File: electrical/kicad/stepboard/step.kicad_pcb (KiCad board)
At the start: 2 copper layers, 139.7 x 76.2 mm, 80 parts, among them J1 Conn_02x03_Odd_Even, J10 Conn_02x03_Odd_Even, J11 Conn_02x03_Odd_Even, J12 Conn_02x03_Odd_Even, J13 Conn_01x04, J14 Conn_01x04, J15 Conn_01x04, J16 Conn_01x04, J17 Conn_01x04, J18 Conn_01x04, J19 Conn_01x04, J2 Conn_02x03_Odd_Even, J20 Conn_01x04, J21 Conn_01x04, J22 Conn_01x04, J23 Conn_01x04, J24 Conn_01x04, J25 Conn_02x12_Odd_Even, J26 Screw_Terminal_01x03, J3 Conn_02x03_Odd_Even, J4 Conn_02x03_Odd_Even, J5 Conn_02x03_Odd_Even, J6 Conn_02x03_Odd_Even, J7 Conn_02x03_Odd_Even, J8 Conn_02x03_Odd_Even, J9 Conn_02x03_Odd_Even, U1 MKS_TMC2209, U10 MKS_TMC2209, U11 MKS_TMC2209, U12 MKS_TMC2209, U2 MKS_TMC2209, U3 MKS_TMC2209, U4 MKS_TMC2209, U5 MKS_TMC2209, U6 MKS_TMC2209, U7 MKS_TMC2209, U8 MKS_TMC2209, U9 MKS_TMC2209

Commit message: update(kicad/pdb): sch with mobility components
- added rover mobility components to schematic
- added overcurrent and flyback protection ckt
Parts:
- J13, J14, J15, J16, J17, J18, J19, J20, J21, J22, J23, J24: footprint Connector_PinHeader_2.54mm:PinHeader_1x04_P2.54mm_Vertical -> Connectors_JST:JST_XH_1x04_P2.54mm_Vertical
- J26: footprint Connector_PinHeader_2.54mm:PinHeader_1x03_P2.54mm_Vertical -> Connectors_JST:JST_XH_1x03_P2.54mm_Vertical

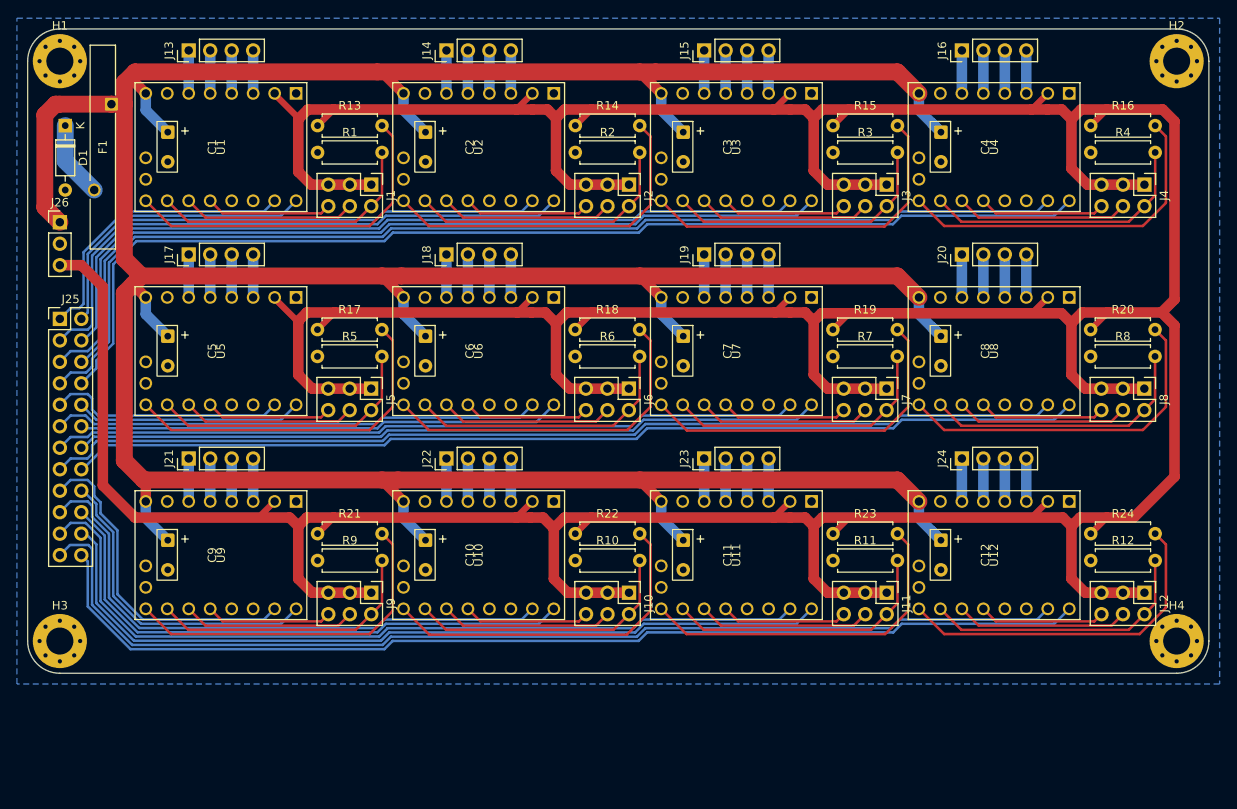
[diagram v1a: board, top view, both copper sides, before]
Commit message: update(kicad/step): reduce from 12 to 9 motors and optimize space
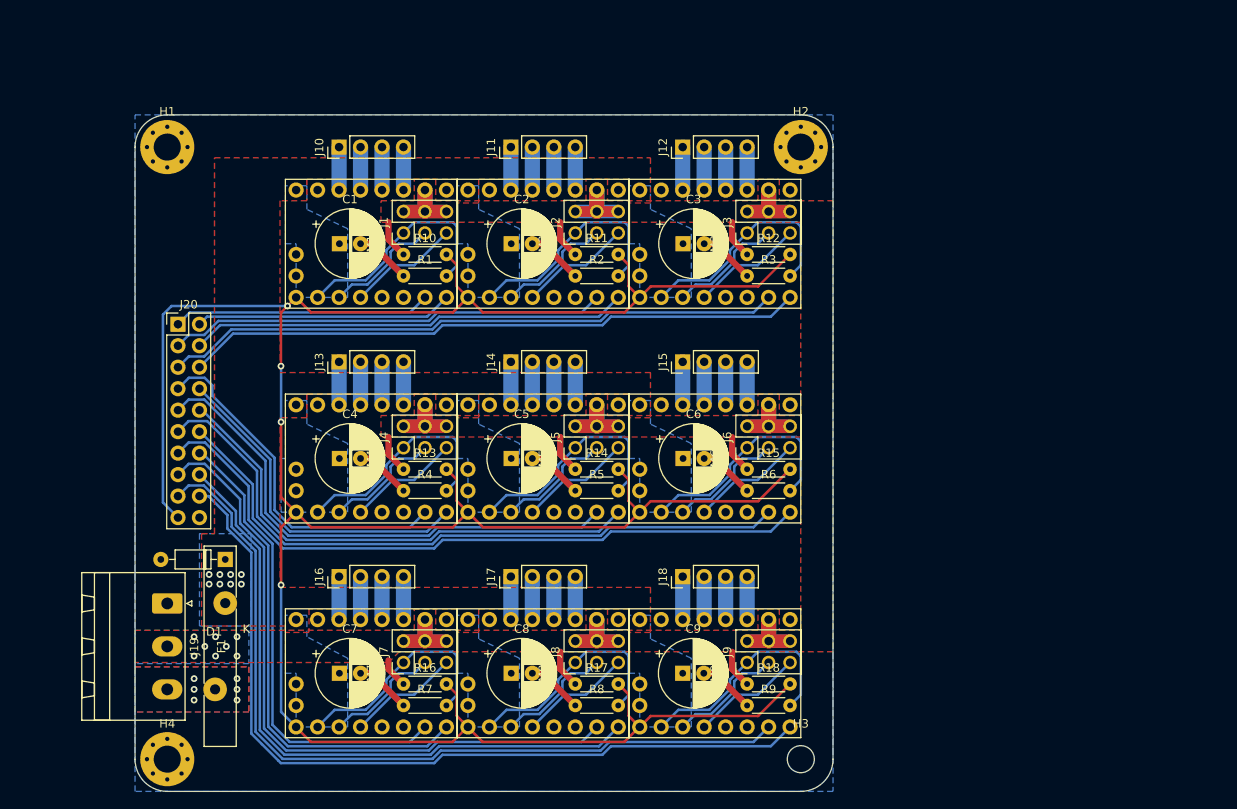
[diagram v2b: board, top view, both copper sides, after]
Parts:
- removed C10, C11, C12: 100uF, Capacitors_THT:CP_Radial_D8.0mm_P3.50mm_H12.0mm_Horizontal
- removed J21, J22, J23, J24: Conn_01x04, Connectors_JST:JST_XH_1x04_P2.54mm_Vertical
- removed J25: Conn_02x12_Odd_Even, Connector_PinHeader_2.54mm:PinHeader_2x12_P2.54mm_Vertical
- removed J26: Screw_Terminal_01x03, Connectors_JST:JST_XH_1x03_P2.54mm_Vertical
- removed R19, R20, R21, R22, R23, R24: 10k, Resistor_THT:R_Axial_DIN0207_L6.3mm_D2.5mm_P7.62mm_Horizontal
- removed U1, U10, U11, U12, U2, U3, U4, U5, U6, U7, U8, U9: MKS_TMC2209, Motor_Driver:MKS_TMC2209
- added M1: TMC22XX, Motor_Driver:MKS_TMC22XX, F.Cu at (62.2, 52.1)
- added M2: TMC22XX, Motor_Driver:MKS_TMC22XX, F.Cu at (82.5, 52.1)
- added M3: TMC22XX, Motor_Driver:MKS_TMC22XX, F.Cu at (102.9, 52.1)
- added M4: TMC22XX, Motor_Driver:MKS_TMC22XX, F.Cu at (62.2, 77.5)
- added M5: TMC22XX, Motor_Driver:MKS_TMC22XX, F.Cu at (82.5, 77.5)
- added M6: TMC22XX, Motor_Driver:MKS_TMC22XX, F.Cu at (102.9, 77.5)
- added M7: TMC22XX, Motor_Driver:MKS_TMC22XX, F.Cu at (62.2, 102.9)
- added M8: TMC22XX, Motor_Driver:MKS_TMC22XX, F.Cu at (82.5, 102.9)
- added M9: TMC22XX, Motor_Driver:MKS_TMC22XX, F.Cu at (102.9, 102.9)
- C1, C2, C3, C4, C5, C6, C7, C8, C9: value 100uF -> 100u; footprint Capacitors_THT:CP_Radial_D8.0mm_P3.50mm_H12.0mm_Horizontal -> Capacitor_THT:CP_Radial_D8.0mm_P2.50mm
- D1: value D -> D_Small
- F1: value Fuse -> Polyfuse_Small; footprint Fuses_THT:Fuse_Tyco-RUEF900 -> Fuses_THT:Fuse_Tyco_RGEF1400
- H3: value MountingHole_Pad -> MountingHole; footprint MountingHole:MountingHole_3.2mm_M3_Pad_Via -> MountingHole:MountingHole_3.2mm_M3
- J10, J11, J12: value Conn_02x03_Odd_Even -> Conn_01x04; footprint Connector_PinHeader_2.54mm:PinHeader_2x03_P2.54mm_Vertical -> Connectors_JST:JST_XH_1x04_P2.54mm_Vertical
- J19: value Conn_01x04 -> Screw_Terminal_01x03; footprint Connectors_JST:JST_XH_1x04_P2.54mm_Vertical -> Connector_Phoenix_MSTB:PhoenixContact_MSTBA_2,5_3-G-5,08_1x03_P5.08mm_Horizontal
- J20: value Conn_01x04 -> Conn_02x10_Odd_Even; footprint Connectors_JST:JST_XH_1x04_P2.54mm_Vertical -> Connector_PinHeader_2.54mm:PinHeader_2x10_P2.54mm_Vertical
- R1, R13, R14, R15, R16, R17, R18, R2, R3, R4, R5, R6, R7, R8, R9: footprint Resistor_THT:R_Axial_DIN0207_L6.3mm_D2.5mm_P7.62mm_Horizontal -> Resistor_THT:R_Axial_DIN0204_L3.6mm_D1.6mm_P5.08mm_Horizontal
- R10, R11, R12: value 100k -> 10k; footprint Resistor_THT:R_Axial_DIN0207_L6.3mm_D2.5mm_P7.62mm_Horizontal -> Resistor_THT:R_Axial_DIN0204_L3.6mm_D1.6mm_P5.08mm_Horizontal
- moved H4 120.2 mm to (38.1, 113.0)
- moved R16 104.7 mm to (66.0, 104.1)
- moved J16 96.4 mm to (58.4, 91.4)
- moved J20 93.1 mm to (39.4, 61.6), turned to 0 degrees
- moved J4 93.0 mm to (66.0, 76.2), turned to 90 degrees
- moved R4 90.6 mm to (66.0, 81.3)
- moved H3 88.7 mm to (113.0, 113.0)
- moved C4 80.9 mm to (58.5, 77.5), turned to 0 degrees
- moved J12 75.9 mm to (99.1, 40.6), turned to 90 degrees
- moved J19 75.7 mm to (38.1, 94.6), turned to -90 degrees
- moved J8 74.7 mm to (86.4, 101.6), turned to 90 degrees
- moved R8 73.6 mm to (86.4, 106.7)
- moved J11 68.9 mm to (78.7, 40.6), turned to 90 degrees
- moved J7 65.7 mm to (66.0, 101.6), turned to 90 degrees
- moved F1 65.5 mm to (43.8, 104.8), turned to 90 degrees
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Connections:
- C1 pad 2: GND -> /GND
- C2 pad 2: GND -> /GND
- C3 pad 2: GND -> /GND
- C4 pad 2: GND -> /GND
- C5 pad 2: GND -> /GND
- C6 pad 2: GND -> /GND
- C7 pad 2: GND -> /GND
- C8 pad 2: GND -> /GND
- C9 pad 2: GND -> /GND
- D1 pad 1: Net-(D1-K) -> /+12V
- D1 pad 2: GND -> /GND
- F1 pad 1: /+12V -> Net-(J19-Pin_3)
- F1 pad 2: Net-(D1-K) -> /+12V
- H1 pad 1: GND -> /GND
- H2 pad 1: GND -> /GND
- H4 pad 1: GND -> /GND
- J1 pad 1: +5V -> Net-(J1-Pin_1)
- J1 pad 2: Net-(J1-Pin_2) -> /+5V
- J1 pad 3: +5V -> Net-(J1-Pin_3)
- J1 pad 4: Net-(J1-Pin_4) -> /+5V
- J1 pad 5: +5V -> Net-(J1-Pin_5)
- J1 pad 6: Net-(J1-Pin_6) -> /+5V
- J10 pad 1: +5V -> Net-(J10-Pin_1)
- J10 pad 3: +5V -> Net-(J10-Pin_3)
- J11 pad 1: +5V -> Net-(J11-Pin_1)
- J11 pad 3: +5V -> Net-(J11-Pin_3)
- J12 pad 1: +5V -> Net-(J12-Pin_1)
- J12 pad 3: +5V -> Net-(J12-Pin_3)
- J19 pad 1: Net-(J19-Pin_1) -> /GND
- J19 pad 2: Net-(J19-Pin_2) -> /+5V
- J2 pad 1: +5V -> Net-(J2-Pin_1)
- J2 pad 2: Net-(J2-Pin_2) -> /+5V
- J2 pad 3: +5V -> Net-(J2-Pin_3)
- J2 pad 4: Net-(J2-Pin_4) -> /+5V
- J2 pad 5: +5V -> Net-(J2-Pin_5)
- J2 pad 6: Net-(J2-Pin_6) -> /+5V
- J20 pad 1: Net-(J20-Pin_1) -> /ST1_STP
- J20 pad 2: Net-(J20-Pin_2) -> /ST1_DIR
- J20 pad 3: Net-(J20-Pin_3) -> /ST2_STP
- J20 pad 4: Net-(J20-Pin_4) -> /ST2_DIR
- J3 pad 1: +5V -> Net-(J3-Pin_1)
- J3 pad 2: Net-(J3-Pin_2) -> /+5V
- J3 pad 3: +5V -> Net-(J3-Pin_3)
- J3 pad 4: Net-(J3-Pin_4) -> /+5V
- J3 pad 5: +5V -> Net-(J3-Pin_5)
- J3 pad 6: Net-(J3-Pin_6) -> /+5V
- J4 pad 1: +5V -> Net-(J4-Pin_1)
- J4 pad 2: Net-(J4-Pin_2) -> /+5V
- J4 pad 3: +5V -> Net-(J4-Pin_3)
- J4 pad 4: Net-(J4-Pin_4) -> /+5V
- J4 pad 5: +5V -> Net-(J4-Pin_5)
- J4 pad 6: Net-(J4-Pin_6) -> /+5V
- J5 pad 1: +5V -> Net-(J5-Pin_1)
- J5 pad 2: Net-(J5-Pin_2) -> /+5V
- J5 pad 3: +5V -> Net-(J5-Pin_3)
- J5 pad 4: Net-(J5-Pin_4) -> /+5V
- J5 pad 5: +5V -> Net-(J5-Pin_5)
- J5 pad 6: Net-(J5-Pin_6) -> /+5V
- J6 pad 1: +5V -> Net-(J6-Pin_1)
- J6 pad 2: Net-(J6-Pin_2) -> /+5V
- J6 pad 3: +5V -> Net-(J6-Pin_3)
- J6 pad 4: Net-(J6-Pin_4) -> /+5V
- J6 pad 5: +5V -> Net-(J6-Pin_5)
- J6 pad 6: Net-(J6-Pin_6) -> /+5V
- J7 pad 1: +5V -> Net-(J7-Pin_1)
- J7 pad 2: Net-(J7-Pin_2) -> /+5V
- J7 pad 3: +5V -> Net-(J7-Pin_3)
- J7 pad 4: Net-(J7-Pin_4) -> /+5V
- J7 pad 5: +5V -> Net-(J7-Pin_5)
- J7 pad 6: Net-(J7-Pin_6) -> /+5V
- J8 pad 1: +5V -> Net-(J8-Pin_1)
- J8 pad 2: Net-(J8-Pin_2) -> /+5V
- J8 pad 3: +5V -> Net-(J8-Pin_3)
- J8 pad 4: Net-(J8-Pin_4) -> /+5V
- J8 pad 5: +5V -> Net-(J8-Pin_5)
- J8 pad 6: Net-(J8-Pin_6) -> /+5V
- J9 pad 1: +5V -> Net-(J9-Pin_1)
- J9 pad 2: Net-(J9-Pin_2) -> /+5V
- J9 pad 3: +5V -> Net-(J9-Pin_3)
- J9 pad 4: Net-(J9-Pin_4) -> /+5V
- J9 pad 5: +5V -> Net-(J9-Pin_5)
- J9 pad 6: Net-(J9-Pin_6) -> /+5V
- R1 pad 1: GND -> /GND
- R1 pad 2: Net-(J1-Pin_2) -> Net-(J1-Pin_1)
- R10 pad 1: GND -> /+5V
- R10 pad 2: Net-(J10-Pin_2) -> /STP_ENA
- R11 pad 1: GND -> /+5V
- R11 pad 2: Net-(J11-Pin_2) -> /STP_ENA
- R12 pad 1: GND -> /+5V
- R12 pad 2: Net-(J12-Pin_2) -> /STP_ENA
- R13 pad 1: +5V -> /+5V
- R13 pad 2: Net-(U1-~{EN}) -> /STP_ENA
- R14 pad 1: +5V -> /+5V
- R14 pad 2: Net-(U2-~{EN}) -> /STP_ENA
- R15 pad 1: +5V -> /+5V
- R15 pad 2: Net-(U3-~{EN}) -> /STP_ENA
- R16 pad 1: +5V -> /+5V
- R16 pad 2: Net-(U4-~{EN}) -> /STP_ENA
- R17 pad 1: +5V -> /+5V
- R17 pad 2: Net-(U5-~{EN}) -> /STP_ENA
- R18 pad 1: +5V -> /+5V
- R18 pad 2: Net-(U6-~{EN}) -> /STP_ENA
- R2 pad 1: GND -> /GND
- R2 pad 2: Net-(J2-Pin_2) -> Net-(J2-Pin_1)
- R3 pad 1: GND -> /GND
- R3 pad 2: Net-(J3-Pin_2) -> Net-(J3-Pin_1)
- R4 pad 1: GND -> /GND
- R4 pad 2: Net-(J4-Pin_2) -> Net-(J4-Pin_1)
- R5 pad 1: GND -> /GND
- R5 pad 2: Net-(J5-Pin_2) -> Net-(J5-Pin_1)
- R6 pad 1: GND -> /GND
- R6 pad 2: Net-(J6-Pin_2) -> Net-(J6-Pin_1)
- R7 pad 1: GND -> /GND
- R7 pad 2: Net-(J7-Pin_2) -> Net-(J7-Pin_1)
- R8 pad 1: GND -> /GND
- R8 pad 2: Net-(J8-Pin_2) -> Net-(J8-Pin_1)
- R9 pad 1: GND -> /GND
- R9 pad 2: Net-(J9-Pin_2) -> Net-(J9-Pin_1)
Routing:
- net +5V: track 673.0 -> 0.00 mm
- net /+12V: track 456.1 -> 0.00 mm, vias 0 -> 8
- net /STP_ENA: track 0.00 -> 320.9 mm, vias 0 -> 4
- net /+5V: track 0.00 -> 187.0 mm, vias 0 -> 8
- net /ST12_STP: track 127.9 -> 0.00 mm
- net /ST12_DIR: track 126.5 -> 0.00 mm
- net /ST11_STP: track 98.2 -> 0.00 mm
- net /ST11_DIR: track 96.7 -> 0.00 mm
- net /ST4_DIR: track 131.8 -> 40.8 mm
- net /ST4_STP: track 131.8 -> 42.1 mm
- net /ST10_STP: track 68.8 -> 0.00 mm
- net /ST10_DIR: track 67.3 -> 0.00 mm
- net /GND: track 0.00 -> 60.7 mm
- net /ST9_DIR: track 37.7 -> 98.2 mm
- net /ST9_STP: track 39.2 -> 98.8 mm
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- added copper zone on B.Cu, net /+12V
- added copper zone on F.Cu, net /+12V
- added copper zone on B.Cu, net /+5V
- added copper zone on F.Cu, net /+5V
- added copper zone on B.Cu, net /GND
- added copper zone on B.Cu, net Net-(J19-Pin_3)
- added copper zone on F.Cu, net Net-(J19-Pin_3)
- removed copper zone on B.Cu, net GND
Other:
- board size 139.7 x 76.2 mm -> 82.6 x 80 mm
